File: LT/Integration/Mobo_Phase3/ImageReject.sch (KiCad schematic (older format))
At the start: 6 parts

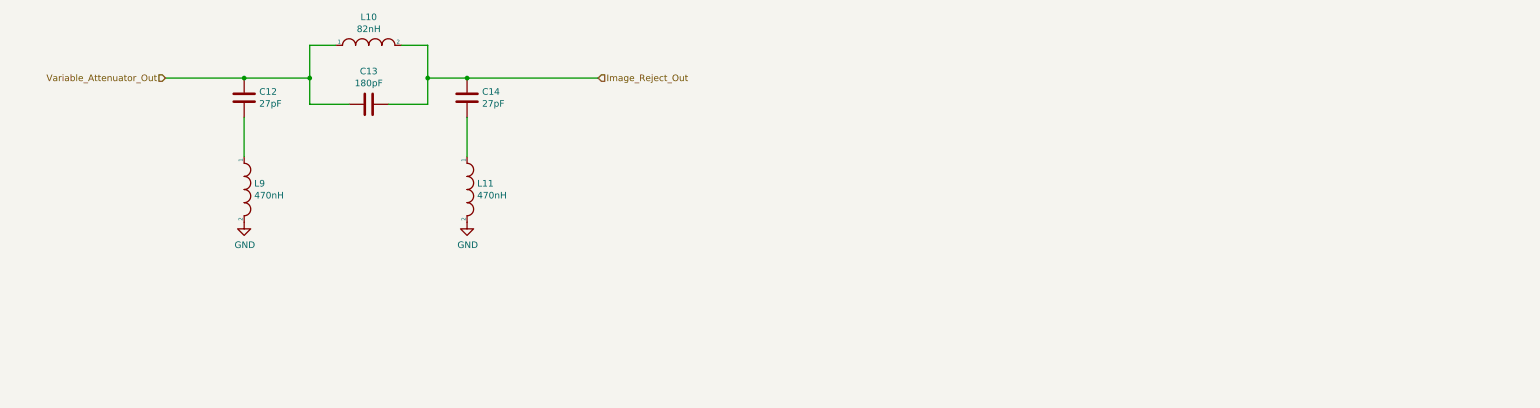
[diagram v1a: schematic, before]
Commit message: Finished the preliminary layout of the receiving stage for MoBo Phase 3
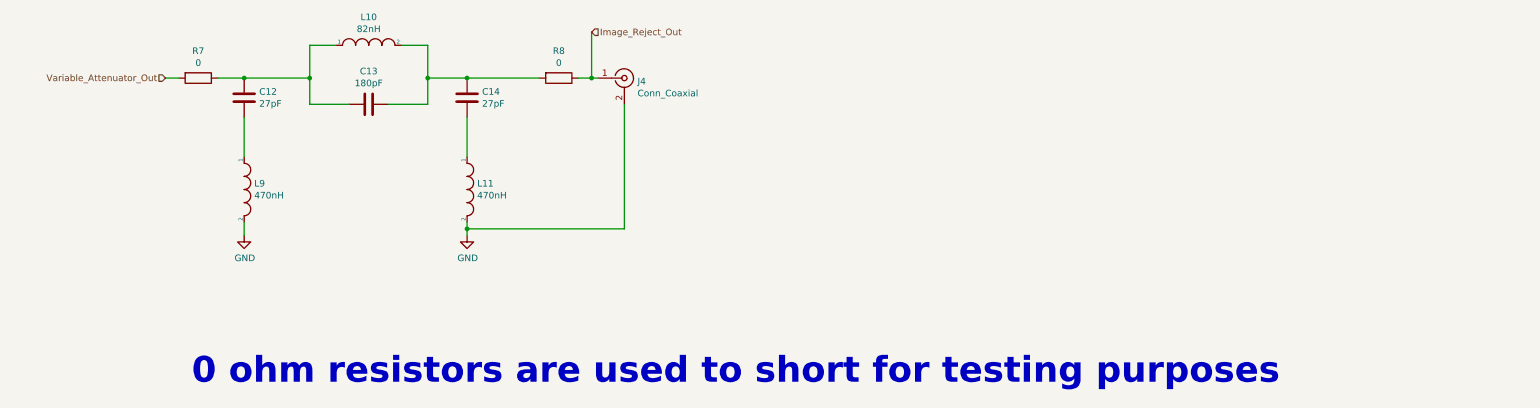
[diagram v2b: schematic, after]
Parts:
- added J4: Conn_Coaxial, Connector_Coaxial:SMA_Amphenol_132291_Vertical, symbol Connector:Conn_Coaxial
- added R7, R8: 0, Resistor_SMD:R_0805_2012Metric_Pad1.15x1.40mm_HandSolder, symbol Device:R
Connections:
- net GND: now also J4.2 (Ext)
- net Image_Reject_Out: now also J4.1 (In), R8.1; no longer C13.1, C14.1, L10.2
- net Variable_Attenuator_Out: now also R7.2; no longer C12.1, C13.2, L10.1
- new net: C12.1, C13.2, L10.1, R7.1
- new net: C13.1, C14.1, L10.2, R8.2
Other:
- note added: "0 ohm resistors are used to short for testing purposes"
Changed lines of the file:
@@
 EESchema Schematic File Version 4
-LIBS:Mobo_Phase3-cache
-EELAYER 26 0
+EELAYER 30 0
 EELAYER END
 $Descr A4 11693 8268
@@
 L power:GND #PWR010
 U 1 1 5CAD1657
-P 3900 3200
-F 0 "#PWR010" H 3900 2950 50  0001 C CNN
-F 1 "GND" H 3905 3027 50  0000 C CNN
-F 2 "" H 3900 3200 50  0001 C CNN
-F 3 "" H 3900 3200 50  0001 C CNN
-	1    3900 3200
+P 3900 3300
+F 0 "#PWR010" H 3900 3050 50  0001 C CNN
+F 1 "GND" H 3905 3127 50  0000 C CNN
+F 2 "" H 3900 3300 50  0001 C CNN
+F 3 "" H 3900 3300 50  0001 C CNN
+	1    3900 3300
 	1    0    0    -1
 $EndComp
@@
 L power:GND #PWR09
 U 1 1 5CAD1681
-P 2200 3200
-F 0 "#PWR09" H 2200 2950 50  0001 C CNN
-F 1 "GND" H 2205 3027 50  0000 C CNN
-F 2 "" H 2200 3200 50  0001 C CNN
-F 3 "" H 2200 3200 50  0001 C CNN
-	1    2200 3200
+P 2200 3300
+F 0 "#PWR09" H 2200 3050 50  0001 C CNN
+F 1 "GND" H 2205 3127 50  0000 C CNN
+F 2 "" H 2200 3300 50  0001 C CNN
+F 3 "" H 2200 3300 50  0001 C CNN
+	1    2200 3300
 	1    0    0    -1
 $EndComp
@@
 Text HLabel 1600 2100 0    50   Input ~ 0
 Variable_Attenuator_Out
-Text HLabel 4900 2100 2    50   Input ~ 0
+Text HLabel 4850 1750 2    50   Input ~ 0
 Image_Reject_Out
 Connection ~ 2200 2100
 Wire Wire Line
-	1600 2100 2200 2100
+	1600 2100 1700 2100
 Wire Wire Line
-	3900 2100 4900 2100
+	3900 2100 4450 2100
+$Comp
+L Device:R R7
+U 1 1 5EB33475
+P 1850 2100
+F 0 "R7" V 1643 2100 50  0000 C CNN
+F 1 "0" V 1734 2100 50  0000 C CNN
+F 2 "Resistor_SMD:R_0805_2012Metric_Pad1.15x1.40mm_HandSolder" V 1780 2100 50  0001 C CNN
+F 3 "~" H 1850 2100 50  0001 C CNN
+	1    1850 2100
+	0    1    1    0
+$EndComp
+Wire Wire Line
+	2000 2100 2200 2100
+$Comp
+L Connector:Conn_Coaxial J4
+U 1 1 5EB340A3
+P 5100 2100
+F 0 "J4" H 5200 2075 50  0000 L CNN
+F 1 "Conn_Coaxial" H 5200 1984 50  0000 L CNN
+F 2 "Connector_Coaxial:SMA_Amphenol_132291_Vertical" H 5100 2100 50  0001 C CNN
+F 3 " ~" H 5100 2100 50  0001 C CNN
+	1    5100 2100
+	1    0    0    -1
+$EndComp
+Wire Wire Line
+	4850 1750 4850 2100
+Connection ~ 4850 2100
+Wire Wire Line
+	4850 2100 4900 2100
+Wire Wire Line
+	2200 3200 2200 3300
+Wire Wire Line
+	3900 3200 3900 3250
+Wire Wire Line
+	5100 2300 5100 3250
+Wire Wire Line
+	5100 3250 3900 3250
+Connection ~ 3900 3250
+Wire Wire Line
+	3900 3250 3900 3300
+$Comp
+L Device:R R8
+U 1 1 5EB36333
+P 4600 2100
+F 0 "R8" V 4393 2100 50  0000 C CNN
+F 1 "0" V 4484 2100 50  0000 C CNN
+F 2 "Resistor_SMD:R_0805_2012Metric_Pad1.15x1.40mm_HandSolder" V 4530 2100 50  0001 C CNN
+F 3 "~" H 4600 2100 50  0001 C CNN
+	1    4600 2100
+	0    1    1    0
+$EndComp
+Wire Wire Line
+	4750 2100 4850 2100
+Text Notes 1800 4450 0    197  ~ 39
+0 ohm resistors are used to short for testing purposes
 $EndSCHEMATC

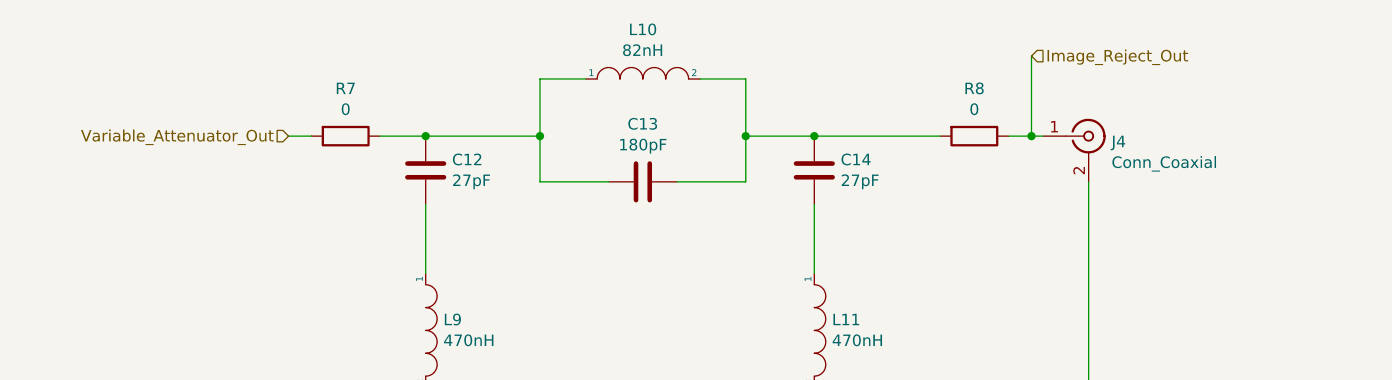
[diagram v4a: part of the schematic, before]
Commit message: Added the finalized layouts for the Mobo and Dobo Phase 3, as well as the preliminary layout for Phase 4 of both boards
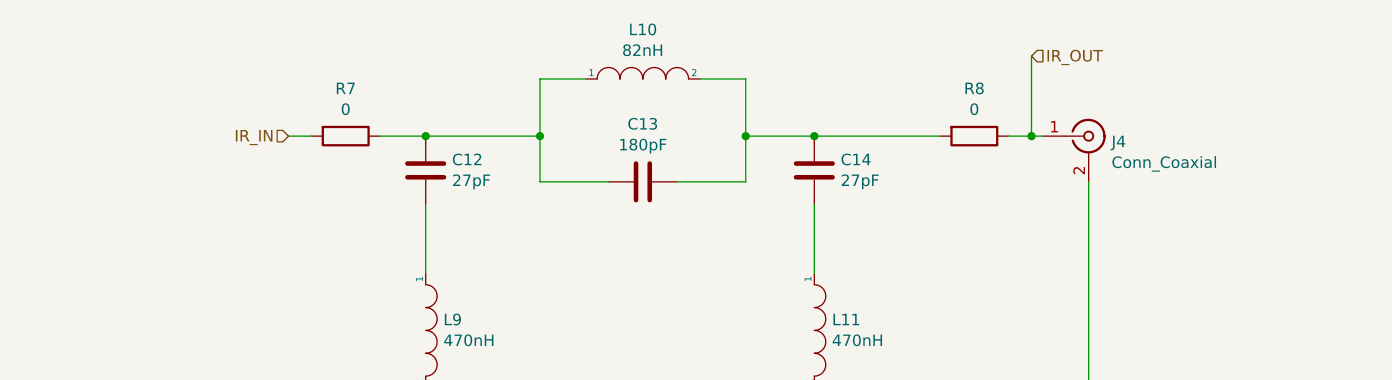
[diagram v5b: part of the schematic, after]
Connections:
- net Image_Reject_Out renamed IR_OUT
- net Variable_Attenuator_Out renamed IR_IN
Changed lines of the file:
@@
 Connection ~ 3900 2100
 Text HLabel 1600 2100 0    50   Input ~ 0
-Variable_Attenuator_Out
+IR_IN
 Text HLabel 4850 1750 2    50   Input ~ 0
-Image_Reject_Out
+IR_OUT
 Connection ~ 2200 2100
 Wire Wire Line
